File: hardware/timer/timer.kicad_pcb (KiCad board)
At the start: 2 copper layers, 86 x 75 mm, 28 parts, among them J1 Conn_01x24_Male, J2 Conn_01x02_Male, J3 Conn_01x24_Male

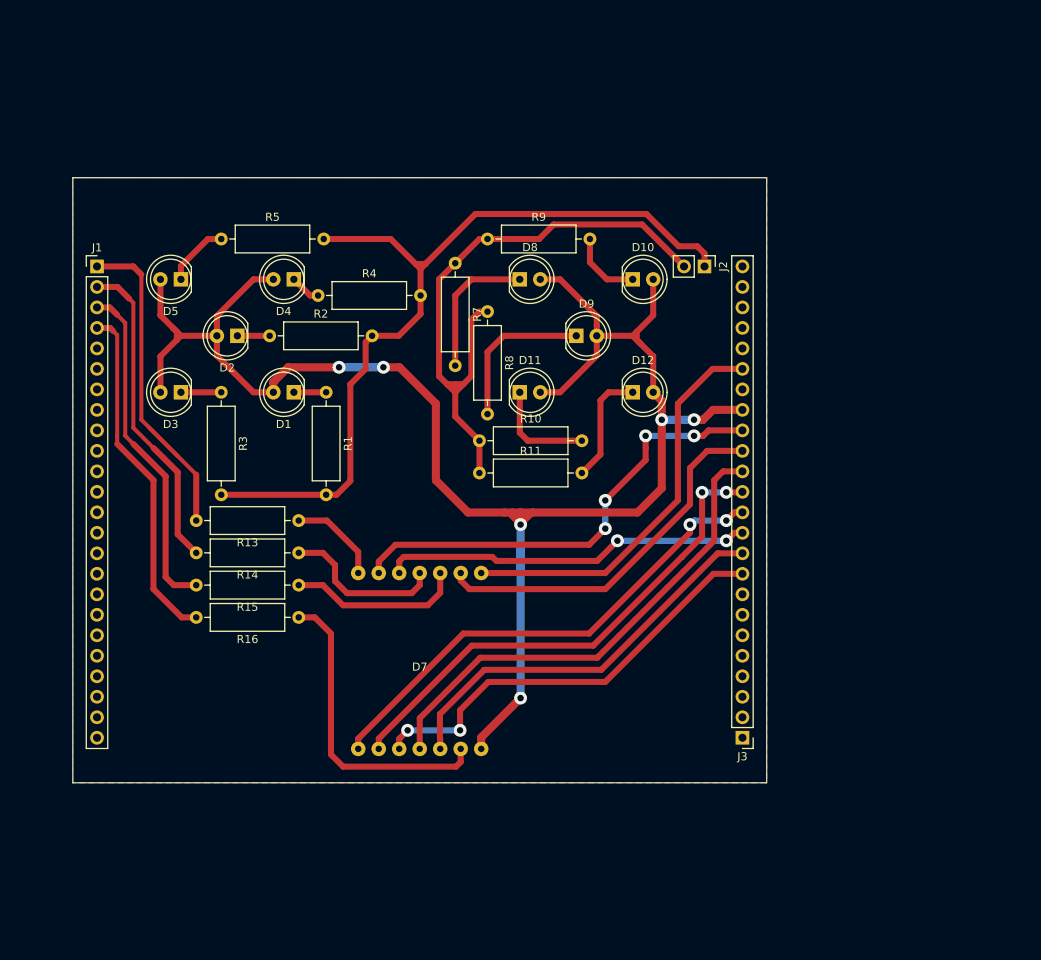
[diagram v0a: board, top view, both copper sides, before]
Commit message: Recreate timer module with single PCB, clean up libraries
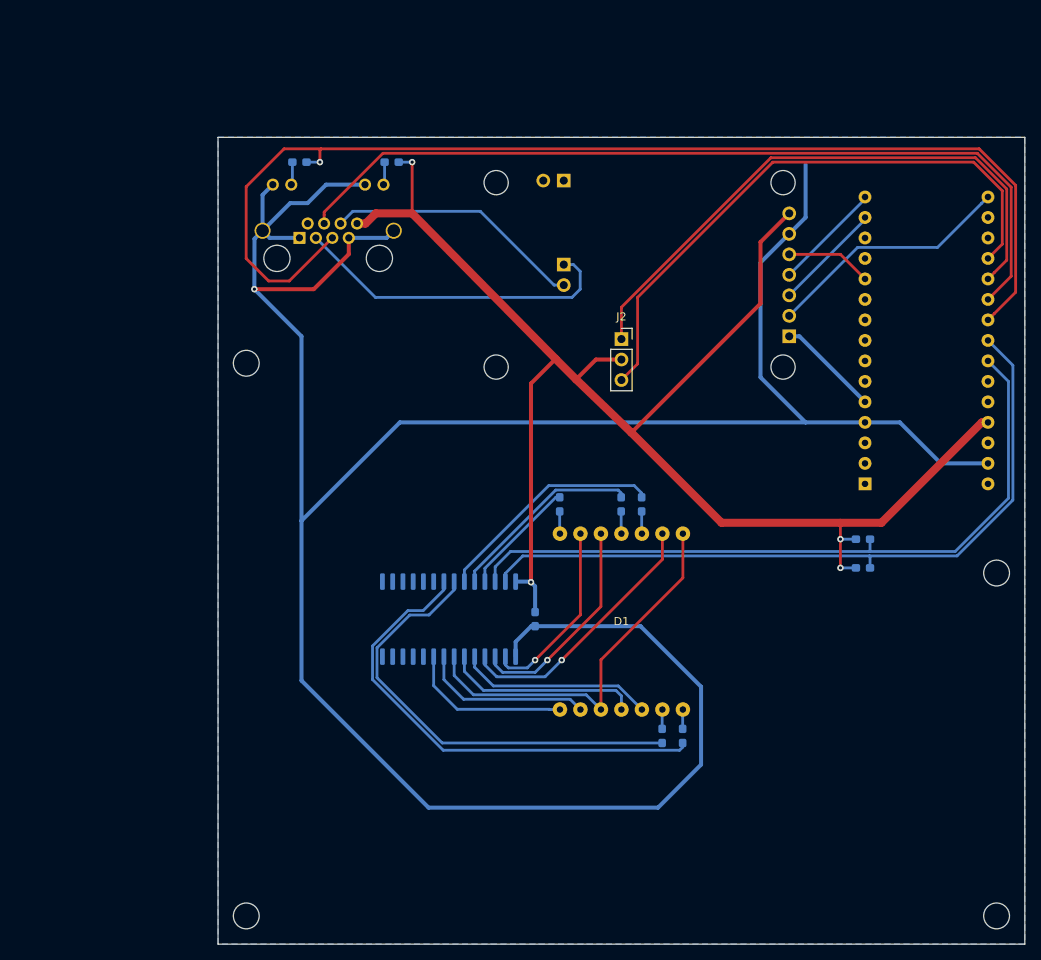
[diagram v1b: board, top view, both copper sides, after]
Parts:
- removed D10, D11, D12, D2, D3, D4, D5, D8, D9: LED, LED_THT:LED_D5.0mm
- removed D7: 8402BS, 8402BS:8042BS
- removed J3: Conn_01x24_Male, Connector_PinHeader_2.54mm:PinHeader_1x24_P2.54mm_Vertical
- removed R10, R11, R13, R14, R15, R16: R, Resistor_THT:R_Axial_DIN0309_L9.0mm_D3.2mm_P12.70mm_Horizontal
- added A1: Arduino_Nano_v3.x, Module:Arduino_Nano, B.Cu at (155.2, 108.0)
- added C1: 0.1uF, Capacitor_SMD:C_0603_1608Metric_Pad1.05x0.95mm_HandSolder, B.Cu at (114.3, 124.7)
- added R6: 100, Resistor_SMD:R_0603_1608Metric_Pad1.05x0.95mm_HandSolder, B.Cu at (125.0, 110.5)
- added REF**: MountingHole_3.2mm_M3, MountingHole:MountingHole_3.2mm_M3, F.Cu at (78.5, 93.0)
- added REF**: MountingHole_3.2mm_M3, MountingHole:MountingHole_3.2mm_M3, F.Cu at (171.5, 119.0)
- added REF**: MountingHole_3.2mm_M3, MountingHole:MountingHole_3.2mm_M3, F.Cu at (171.5, 161.5)
- added REF**: MountingHole_3.2mm_M3, MountingHole:MountingHole_3.2mm_M3, F.Cu at (78.5, 161.5)
- added U1: WAVGAT_CAN, WAVGAT_CAN:WAVGAT_CAN, B.Cu at (137.2, 65.3)
- added U2: HT16K33, Package_SO:SOIC-28W_7.5x17.9mm_P1.27mm, B.Cu at (103.6, 124.7)
- D1: value LED -> 8402BS; footprint LED_THT:LED_D5.0mm -> ProjectDisplays:8042BS
- J1: value Conn_01x24_Male -> RJ45_LED_Shielded; footprint Connector_PinHeader_2.54mm:PinHeader_1x24_P2.54mm_Vertical -> Connector_RJ:RJ45_Amphenol_RJHSE538X; moved to B.Cu
- J2: value Conn_01x02_Male -> Conn_01x03_Female; footprint Connector_PinHeader_2.54mm:PinHeader_1x02_P2.54mm_Vertical -> Connector_PinSocket_2.54mm:PinSocket_1x03_P2.54mm_Vertical
- R1, R2: value R -> 560R; footprint Resistor_THT:R_Axial_DIN0309_L9.0mm_D3.2mm_P12.70mm_Horizontal -> Resistor_SMD:R_0603_1608Metric_Pad1.05x0.95mm_HandSolder; moved to B.Cu
- R3, R4: value R -> 4K7; footprint Resistor_THT:R_Axial_DIN0309_L9.0mm_D3.2mm_P12.70mm_Horizontal -> Resistor_SMD:R_0603_1608Metric_Pad1.05x0.95mm_HandSolder; moved to B.Cu
- R5, R7, R8, R9: value R -> 100; footprint Resistor_THT:R_Axial_DIN0309_L9.0mm_D3.2mm_P12.70mm_Horizontal -> Resistor_SMD:R_0603_1608Metric_Pad1.05x0.95mm_HandSolder; moved to B.Cu
- moved R3 82.5 mm to (154.9, 118.4), turned to 180 degrees
- moved R4 74.0 mm to (154.9, 114.8), turned to 180 degrees
- moved R9 66.2 mm to (132.6, 139.2), turned to 270 degrees
- moved R8 56.9 mm to (130.0, 139.2)
- moved R5 53.3 mm to (117.3, 110.5), turned to 90 degrees
- moved D1 49.5 mm to (125.0, 125.0), turned to 0 degrees
- moved R7 37.8 mm to (127.5, 110.5), turned to 90 degrees
- moved R1 29.7 mm to (96.5, 68.1), turned to 180 degrees
- moved J1 25.3 mm to (85.1, 77.5)
- moved R2 21.8 mm to (85.1, 68.1)
- moved J2 13.7 mm to (125.0, 90.0), turned to 0 degrees
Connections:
- J1 pad 1: Net-(J1-Pad1) -> GND
- J1 pad 10: (no net) -> Net-(J1-Pad10)
- J1 pad 11: (no net) -> GND
- J1 pad 12: (no net) -> Net-(J1-Pad12)
- J1 pad 2: Net-(J1-Pad2) -> +12V
- J1 pad 4: Net-(J1-Pad4) -> MODULE_READY
- J1 pad 5: (no net) -> MODULE_ENABLE
- J1 pad 6: (no net) -> Net-(J1-Pad6)
- J1 pad 7: (no net) -> GND
- J1 pad 8: (no net) -> VCC
- J1 pad 9: (no net) -> GND
- J2 pad 1: Net-(J2-Pad1) -> A1
- J2 pad 2: Net-(J2-Pad2) -> VCC
- R1 pad 1: Net-(D1-Pad1) -> VCC
- R1 pad 2: Net-(J2-Pad1) -> Net-(J1-Pad12)
- R2 pad 1: Net-(D2-Pad1) -> Net-(J1-Pad10)
- R2 pad 2: Net-(J2-Pad1) -> MODULE_ENABLE
- R3 pad 1: Net-(D3-Pad1) -> A4_SDA
- R3 pad 2: Net-(J2-Pad1) -> VCC
- R4 pad 1: Net-(D4-Pad1) -> A5_SCL
- R4 pad 2: Net-(J2-Pad1) -> VCC
- R5 pad 1: Net-(D5-Pad1) -> Net-(D1-Pad14)
- R5 pad 2: Net-(J2-Pad1) -> Net-(R5-Pad2)
- R7 pad 1: Net-(J2-Pad2) -> Net-(D1-Pad10)
- R8 pad 1: Net-(J2-Pad2) -> Net-(D1-Pad6)
- R9 pad 1: Net-(J2-Pad2) -> Net-(D1-Pad7)
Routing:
- net GND: track 0.00 -> 331.8 mm, vias 0 -> 1
- net Net-(D1-Pad2): track 217.0 -> 21.3 mm, vias 6 -> 0
- net VCC: track 0.00 -> 193.9 mm, vias 0 -> 4
- net MODULE_ENABLE: track 0.00 -> 143.6 mm, vias 0 -> 1
- net MODULE_READY: track 0.00 -> 106.4 mm
- net Net-(J2-Pad1): track 105.1 -> 0.00 mm
- net A4_SDA: track 0.00 -> 90.3 mm
- net A5_SCL: track 0.00 -> 88.6 mm
- net Net-(J2-Pad2): track 76.6 -> 0.00 mm
- net A0: track 0.00 -> 73.8 mm
- net A1: track 0.00 -> 73.1 mm
- net Net-(D7-Pad2): track 62.2 -> 0.00 mm, vias 2 -> 0
- net Net-(D7-Pad1): track 61.1 -> 0.00 mm, vias 2 -> 0
- net Net-(D7-Pad4): track 60.9 -> 0.00 mm
- net Net-(D7-Pad13): track 57.0 -> 0.00 mm, vias 4 -> 0
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- added copper zone on B.Cu, net GND
- removed copper zone on F.Cu, net (none)
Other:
- board size 86 x 75 mm -> 100 x 100 mm

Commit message: Timer PCB: use non-LED RJ45, update layout, reroute
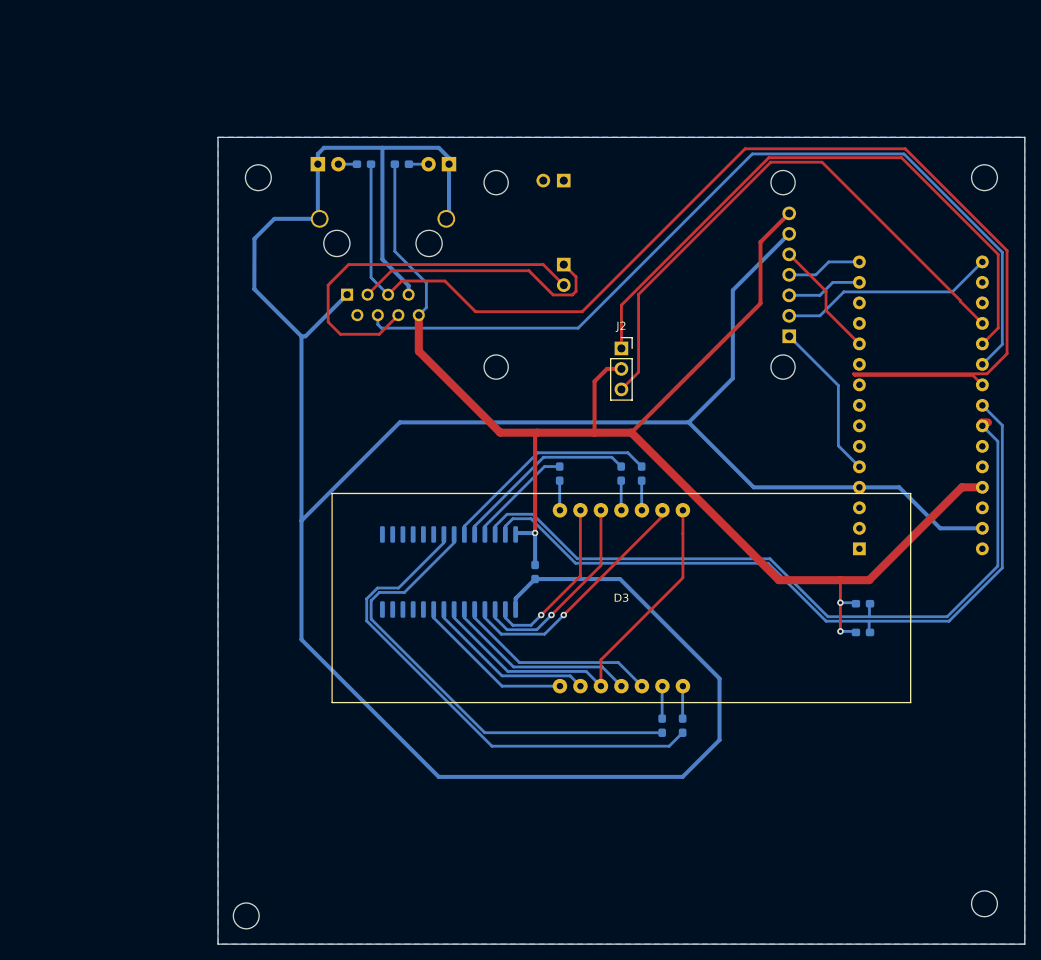
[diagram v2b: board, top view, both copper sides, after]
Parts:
- removed the REF** at (171.5, 119.0)
- removed the REF** at (171.5, 161.5)
- added D2: LED_Small, LED_THT:LED_D3.0mm, B.Cu at (103.6, 68.3)
- added D3: 8402BS, ProjectDisplays:8402BS, F.Cu at (125.0, 122.1)
- added REF**: MountingHole_3.2mm_M3, MountingHole:MountingHole_3.2mm_M3, F.Cu at (170.0, 70.0)
- added REF**: MountingHole_3.2mm_M3, MountingHole:MountingHole_3.2mm_M3, F.Cu at (170.0, 160.0)
- D1: value 8402BS -> LED_Small; footprint ProjectDisplays:8042BS -> LED_THT:LED_D3.0mm; moved to B.Cu
- J1: value RJ45_LED_Shielded -> RJ45_Shielded; footprint Connector_RJ:RJ45_Amphenol_RJHSE538X -> RJ45_5224:RJ45_5224
- moved D1 68.0 mm to (87.4, 68.3)
- moved REF** 23.0 mm to (80.0, 70.0)
- moved J1 9.19 mm to (91.0, 84.5)
- moved A1 8.08 mm to (154.5, 116.0)
- moved R2 8.01 mm to (93.1, 68.3)
- moved R3 8.00 mm to (154.9, 126.4)
- moved R4 8.00 mm to (154.9, 122.8)
- moved C1 5.84 mm to (114.3, 118.9)
- moved U2 5.84 mm to (103.6, 118.9)
- moved R5 3.81 mm to (117.3, 106.7)
- moved R6 3.81 mm to (125.0, 106.7)
- moved R7 3.81 mm to (127.5, 106.7)
- moved R1 1.30 mm to (97.8, 68.3), turned to 0 degrees
- moved R8 1.27 mm to (130.0, 137.9)
- moved R9 1.27 mm to (132.6, 137.9)
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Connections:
- D1 pad 1: Net-(D1-Pad1) -> GND
- R1 pad 2: Net-(J1-Pad12) -> Net-(D2-Pad2)
- R2 pad 1: Net-(J1-Pad10) -> Net-(D1-Pad2)
- R5 pad 1: Net-(D1-Pad14) -> Net-(D3-Pad14)
- R6 pad 1: Net-(D1-Pad11) -> Net-(D3-Pad11)
- R7 pad 1: Net-(D1-Pad10) -> Net-(D3-Pad10)
- R8 pad 1: Net-(D1-Pad6) -> Net-(D3-Pad6)
- R9 pad 1: Net-(D1-Pad7) -> Net-(D3-Pad7)
- U2 pad 2: Net-(D1-Pad13) -> Net-(D3-Pad13)
- U2 pad 3: Net-(D1-Pad12) -> Net-(D3-Pad12)
- U2 pad 4: Net-(D1-Pad9) -> Net-(D3-Pad9)
- U2 pad 5: Net-(D1-Pad5) -> Net-(D3-Pad5)
- U2 pad 6: Net-(D1-Pad4) -> Net-(D3-Pad4)
- U2 pad 7: Net-(D1-Pad3) -> Net-(D3-Pad3)
- U2 pad 8: Net-(D1-Pad2) -> Net-(D3-Pad2)
- U2 pad 9: Net-(D1-Pad1) -> Net-(D3-Pad1)
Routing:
- net Net-(D3-Pad3): track 0.00 -> 48.7 mm
- net Net-(D1-Pad3): track 48.3 -> 0.00 mm
- net Net-(D1-Pad9): track 32.9 -> 0.00 mm, vias 1 -> 0
- net Net-(D3-Pad9): track 0.00 -> 30.7 mm, vias 0 -> 1
- net Net-(D1-Pad12): track 26.9 -> 0.00 mm, vias 1 -> 0
- net Net-(D3-Pad12): track 0.00 -> 26.0 mm, vias 0 -> 1
- net Net-(D3-Pad5): track 0.00 -> 25.3 mm
- net Net-(D1-Pad4): track 24.2 -> 0.00 mm
- net Net-(D1-Pad5): track 24.2 -> 0.00 mm
- net Net-(D3-Pad4): track 0.00 -> 24.0 mm
- net Net-(D1-Pad13): track 23.3 -> 0.00 mm, vias 1 -> 0
- net Net-(D3-Pad2): track 0.00 -> 21.5 mm
- net Net-(D3-Pad13): track 0.00 -> 21.4 mm, vias 0 -> 1
- net Net-(D1-Pad1): track 20.5 -> 0.00 mm
- net Net-(D3-Pad1): track 0.00 -> 20.2 mm
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
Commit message: Timer PCB: add copper fills
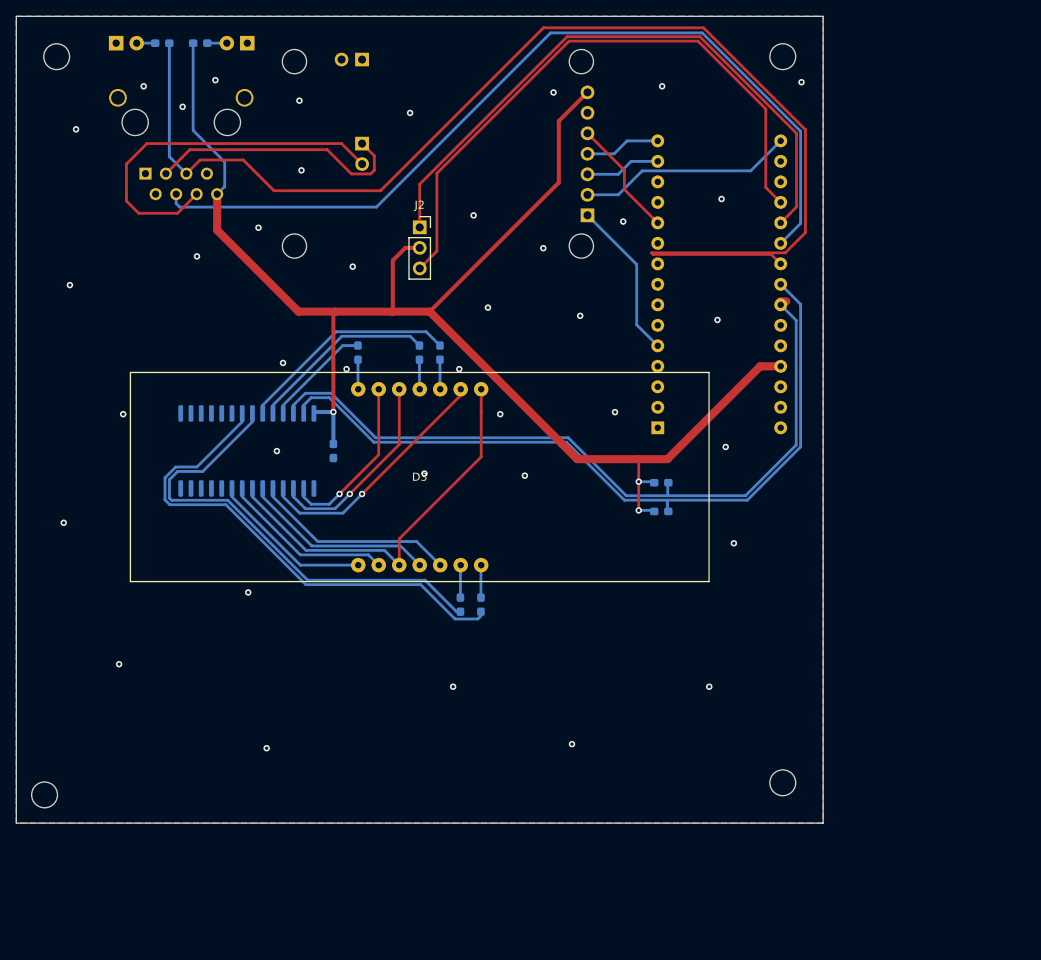
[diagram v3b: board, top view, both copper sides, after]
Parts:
- moved U1 29.2 mm to (112.2, 50.3)
- moved D1 29.2 mm to (62.4, 53.3)
- moved A1 29.2 mm to (129.5, 101.0)
- moved C1 29.2 mm to (89.3, 103.9)
- moved D2 29.2 mm to (78.6, 53.3)
- moved D3 29.2 mm to (100.0, 107.1)
- moved J1 29.2 mm to (66.0, 69.5)
- moved J2 29.2 mm to (100.0, 76.2)
- moved R1 29.2 mm to (72.8, 53.3)
- moved R2 29.2 mm to (68.1, 53.3)
- moved R3 29.2 mm to (129.9, 111.4)
- moved R4 29.2 mm to (129.9, 107.8)
- moved R5 29.2 mm to (92.3, 91.7)
- moved R6 29.2 mm to (100.0, 91.7)
- moved R7 29.2 mm to (102.5, 91.7)
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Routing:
- net GND: track 346.5 -> 0.00 mm, vias 0 -> 39
- net A0: track 70.4 -> 76.1 mm
- added copper zone on F.Cu, net GND
